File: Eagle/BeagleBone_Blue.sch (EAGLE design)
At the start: 152 parts, among them M1 JST_ZH_2, M2 JST_ZH_2, M3 JST_ZH_2, M4 JST_ZH_2, Q3 MOSFET-N, U1 OSD3358

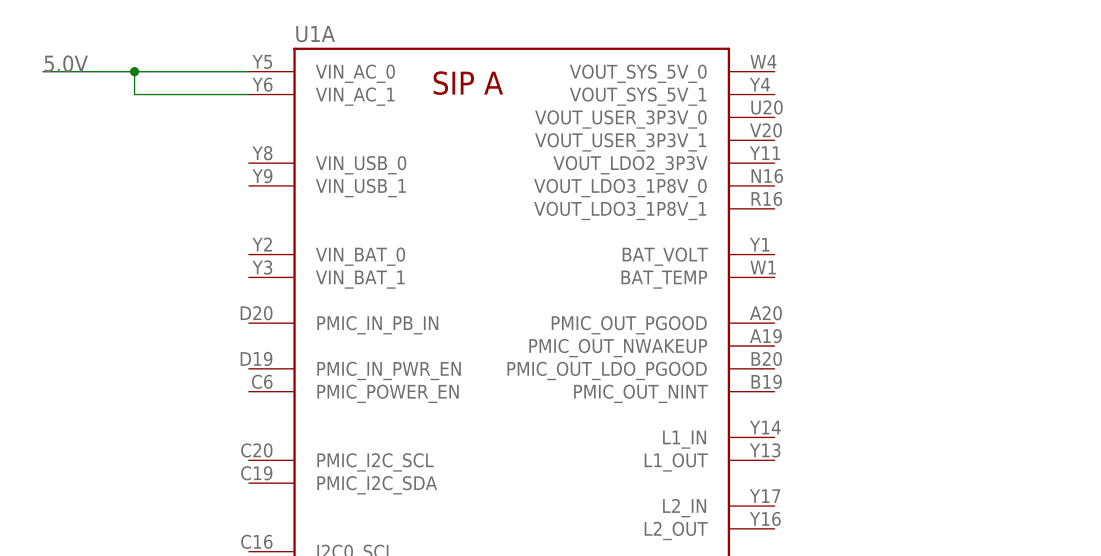
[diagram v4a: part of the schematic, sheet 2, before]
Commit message: Connected PWR button
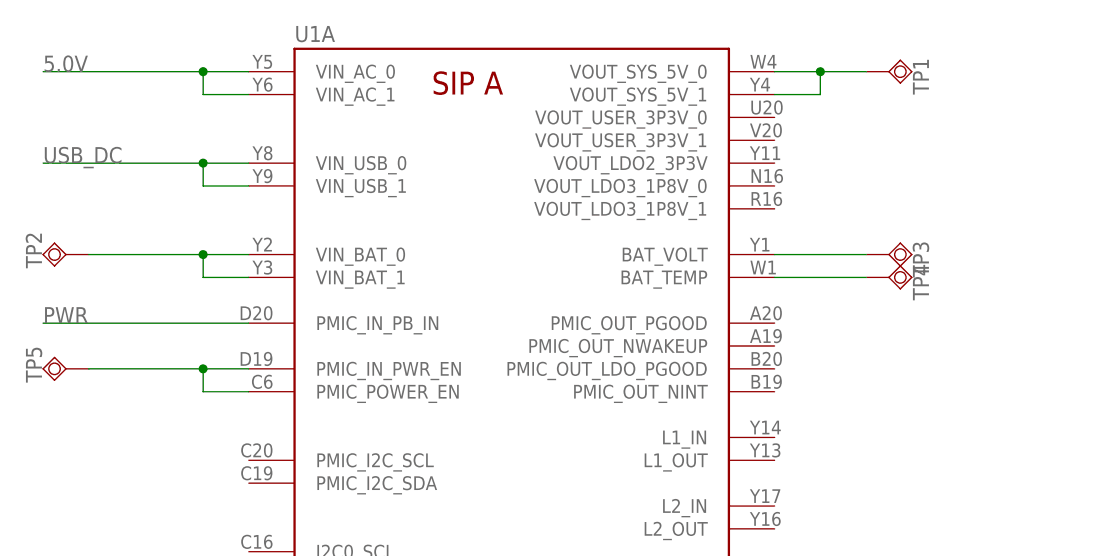
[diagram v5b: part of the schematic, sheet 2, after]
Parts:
- removed U$10, U$11, U$13, U$14, U$15, U$16, U$17, U$18, U$19, U$20, U$21, U$22, U$24, U$25, U$26, U$27, U$28, U$29, U$3, U$30, U$4, U$5, U$7: OSD3358, BeagleBone_Blue:OSD3358
- added TP1, TP2, TP3, TP4, TP5: TPSQB1,27, testpad:TPSQB1,27
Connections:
- new net N$12: TP5.TP, U1A.PMIC_IN_PWR_EN, U1A.PMIC_POWER_EN
- new net N$2: TP1.TP, U1A.VOUT_SYS_5V_0, U1A.VOUT_SYS_5V_1
- new net N$5: TP2.TP, U1A.VIN_BAT_0, U1A.VIN_BAT_1
- new net N$7: TP3.TP, U1A.BAT_VOLT
- new net N$9: TP4.TP, U1A.BAT_TEMP
- new net USB_DC: U1A.VIN_USB_0, U1A.VIN_USB_1
- net PWR: now also U1A.PMIC_IN_PB_IN
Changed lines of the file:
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@@
 <layer number="223" name="223bmp" color="24" fill="1" visible="no" active="no"/>
 <layer number="224" name="224bmp" color="25" fill="1" visible="no" active="no"/>
+<layer number="225" name="225bmp" color="7" fill="1" visible="yes" active="yes"/>
+<layer number="226" name="226bmp" color="7" fill="1" visible="yes" active="yes"/>
+<layer number="227" name="227bmp" color="7" fill="1" visible="yes" active="yes"/>
+<layer number="228" name="228bmp" color="7" fill="1" visible="yes" active="yes"/>
+<layer number="229" name="229bmp" color="7" fill="1" visible="yes" active="yes"/>
+<layer number="230" name="230bmp" color="7" fill="1" visible="yes" active="yes"/>
+<layer number="231" name="231bmp" color="7" fill="1" visible="yes" active="yes"/>
 <layer number="248" name="Housing" color="7" fill="1" visible="yes" active="yes"/>
 <layer number="249" name="Edge" color="7" fill="1" visible="yes" active="yes"/>
@@
 <layer number="251" name="SMDround" color="12" fill="11" visible="no" active="no"/>
 <layer number="254" name="cooling" color="7" fill="1" visible="yes" active="yes"/>
+<layer number="255" name="routoute" color="7" fill="1" visible="yes" active="yes"/>
 </layers>
 <schematic xreflabel="%F%N/%S.%C%R" xrefpart="/%S.%C%R">
@@
 <part name="R8" library="Strawson_Eagle_Lib" deviceset="RESISTOR" device="0402-RES" value="10k"/>
 <part name="GND9" library="SparkFun-Aesthetics" deviceset="GND" device=""/>
-<part name="U$3" library="BeagleBone_Blue" deviceset="OSD3358" device=""/>
-<part name="U$4" library="BeagleBone_Blue" deviceset="OSD3358" device=""/>
-<part name="U$5" library="BeagleBone_Blue" deviceset="OSD3358" device=""/>
-<part name="U$7" library="BeagleBone_Blue" deviceset="OSD3358" device=""/>
-<part name="U$10" library="BeagleBone_Blue" deviceset="OSD3358" device=""/>
-<part name="U$11" library="BeagleBone_Blue" deviceset="OSD3358" device=""/>
-<part name="U$13" library="BeagleBone_Blue" deviceset="OSD3358" device=""/>
-<part name="U$14" library="BeagleBone_Blue" deviceset="OSD3358" device=""/>
-<part name="U$15" library="BeagleBone_Blue" deviceset="OSD3358" device=""/>
-<part name="U$16" library="BeagleBone_Blue" deviceset="OSD3358" device=""/>
-<part name="U$17" library="BeagleBone_Blue" deviceset="OSD3358" device=""/>
-<part name="U$18" library="BeagleBone_Blue" deviceset="OSD3358" device=""/>
-<part name="U$19" library="BeagleBone_Blue" deviceset="OSD3358" device=""/>
-<part name="U$20" library="BeagleBone_Blue" deviceset="OSD3358" device=""/>
-<part name="U$21" library="BeagleBone_Blue" deviceset="OSD3358" device=""/>
-<part name="U$22" library="BeagleBone_Blue" deviceset="OSD3358" device=""/>
-<part name="U$24" library="BeagleBone_Blue" deviceset="OSD3358" device=""/>
-<part name="U$25" library="BeagleBone_Blue" deviceset="OSD3358" device=""/>
-<part name="U$26" library="BeagleBone_Blue" deviceset="OSD3358" device=""/>
-<part name="U$27" library="BeagleBone_Blue" deviceset="OSD3358" device=""/>
-<part name="U$28" library="BeagleBone_Blue" deviceset="OSD3358" device=""/>
-<part name="U$29" library="BeagleBone_Blue" deviceset="OSD3358" device=""/>
-<part name="U$30" library="BeagleBone_Blue" deviceset="OSD3358" device=""/>
 <part name="U1" library="BeagleBone_Blue" deviceset="OSD3358" device=""/>
+<part name="TP1" library="testpad" deviceset="TPSQ" device="B1,27"/>
+<part name="TP2" library="testpad" deviceset="TPSQ" device="B1,27"/>
+<part name="TP3" library="testpad" deviceset="TPSQ" device="B1,27"/>
+<part name="TP4" library="testpad" deviceset="TPSQ" device="B1,27"/>
+<part name="TP5" library="testpad" deviceset="TPSQ" device="B1,27"/>
 </parts>
 <sheets>
@@
 <instance part="U1" gate="A" x="71.12" y="187.96"/>
 <instance part="U1" gate="C" x="71.12" y="33.02"/>
+<instance part="TP1" gate="G$1" x="137.16" y="248.92" rot="R90"/>
+<instance part="TP2" gate="G$1" x="45.72" y="228.6" rot="R270"/>
+<instance part="TP3" gate="G$1" x="137.16" y="228.6" rot="R90"/>
+<instance part="TP4" gate="G$1" x="137.16" y="226.06" rot="R90"/>
+<instance part="TP5" gate="G$1" x="45.72" y="215.9" rot="R270"/>
 </instances>
 <busses>
@@
 <segment>
 <pinref part="U1" gate="A" pin="VIN_AC_0"/>
-<wire x1="66.04" y1="248.92" x2="53.34" y2="248.92" width="0.1524" layer="91"/>
-<wire x1="53.34" y1="248.92" x2="53.34" y2="246.38" width="0.1524" layer="91"/>
+<wire x1="66.04" y1="248.92" x2="60.96" y2="248.92" width="0.1524" layer="91"/>
+<wire x1="60.96" y1="248.92" x2="60.96" y2="246.38" width="0.1524" layer="91"/>
 <pinref part="U1" gate="A" pin="VIN_AC_1"/>
-<wire x1="53.34" y1="246.38" x2="66.04" y2="246.38" width="0.1524" layer="91"/>
-<wire x1="53.34" y1="248.92" x2="43.18" y2="248.92" width="0.1524" layer="91"/>
-<junction x="53.34" y="248.92"/>
+<wire x1="60.96" y1="246.38" x2="66.04" y2="246.38" width="0.1524" layer="91"/>
+<wire x1="60.96" y1="248.92" x2="43.18" y2="248.92" width="0.1524" layer="91"/>
+<junction x="60.96" y="248.92"/>
 <label x="43.18" y="248.92" size="1.778" layer="95"/>
 </segment>
 </net>
+<net name="N$2" class="0">
+<segment>
+<pinref part="U1" gate="A" pin="VOUT_SYS_5V_1"/>
+<wire x1="124.46" y1="246.38" x2="129.54" y2="246.38" width="0.1524" layer="91"/>
+<wire x1="129.54" y1="246.38" x2="129.54" y2="248.92" width="0.1524" layer="91"/>
+<pinref part="U1" gate="A" pin="VOUT_SYS_5V_0"/>
+<wire x1="129.54" y1="248.92" x2="124.46" y2="248.92" width="0.1524" layer="91"/>
+<wire x1="129.54" y1="248.92" x2="134.62" y2="248.92" width="0.1524" layer="91"/>
+<junction x="129.54" y="248.92"/>
+<pinref part="TP1" gate="G$1" pin="TP"/>
+</segment>
+</net>
+<net name="USB_DC" class="0">
+<segment>
+<pinref part="U1" gate="A" pin="VIN_USB_0"/>
+<wire x1="66.04" y1="238.76" x2="60.96" y2="238.76" width="0.1524" layer="91"/>
+<pinref part="U1" gate="A" pin="VIN_USB_1"/>
+<wire x1="60.96" y1="238.76" x2="43.18" y2="238.76" width="0.1524" layer="91"/>
+<wire x1="66.04" y1="236.22" x2="60.96" y2="236.22" width="0.1524" layer="91"/>
+<wire x1="60.96" y1="236.22" x2="60.96" y2="238.76" width="0.1524" layer="91"/>
+<junction x="60.96" y="238.76"/>
+<label x="43.18" y="238.76" size="1.778" layer="95"/>
+</segment>
+</net>
+<net name="N$5" class="0">
+<segment>
+<pinref part="U1" gate="A" pin="VIN_BAT_0"/>
+<wire x1="66.04" y1="228.6" x2="60.96" y2="228.6" width="0.1524" layer="91"/>
+<wire x1="60.96" y1="228.6" x2="48.26" y2="228.6" width="0.1524" layer="91"/>
+<wire x1="60.96" y1="228.6" x2="60.96" y2="226.06" width="0.1524" layer="91"/>
+<junction x="60.96" y="228.6"/>
+<pinref part="U1" gate="A" pin="VIN_BAT_1"/>
+<wire x1="60.96" y1="226.06" x2="66.04" y2="226.06" width="0.1524" layer="91"/>
+<pinref part="TP2" gate="G$1" pin="TP"/>
+</segment>
+</net>
+<net name="N$7" class="0">
+<segment>
+<pinref part="U1" gate="A" pin="BAT_VOLT"/>
+<pinref part="TP3" gate="G$1" pin="TP"/>
+<wire x1="124.46" y1="228.6" x2="134.62" y2="228.6" width="0.1524" layer="91"/>
+</segment>
+</net>
+<net name="N$9" class="0">
+<segment>
+<pinref part="U1" gate="A" pin="BAT_TEMP"/>
+<pinref part="TP4" gate="G$1" pin="TP"/>
+<wire x1="124.46" y1="226.06" x2="134.62" y2="226.06" width="0.1524" layer="91"/>
+</segment>
+</net>
+<net name="N$12" class="0">
+<segment>
+<pinref part="U1" gate="A" pin="PMIC_IN_PWR_EN"/>
+<wire x1="66.04" y1="215.9" x2="60.96" y2="215.9" width="0.1524" layer="91"/>
+<wire x1="60.96" y1="215.9" x2="48.26" y2="215.9" width="0.1524" layer="91"/>
+<wire x1="60.96" y1="215.9" x2="60.96" y2="213.36" width="0.1524" layer="91"/>
+<junction x="60.96" y="215.9"/>
+<pinref part="U1" gate="A" pin="PMIC_POWER_EN"/>
+<wire x1="60.96" y1="213.36" x2="66.04" y2="213.36" width="0.1524" layer="91"/>
+<pinref part="TP5" gate="G$1" pin="TP"/>
+</segment>
+</net>
+<net name="PWR" class="0">
+<segment>
+<pinref part="U1" gate="A" pin="PMIC_IN_PB_IN"/>
+<wire x1="66.04" y1="220.98" x2="43.18" y2="220.98" width="0.1524" layer="91"/>
+<label x="43.18" y="220.98" size="1.778" layer="95"/>
+</segment>
+</net>

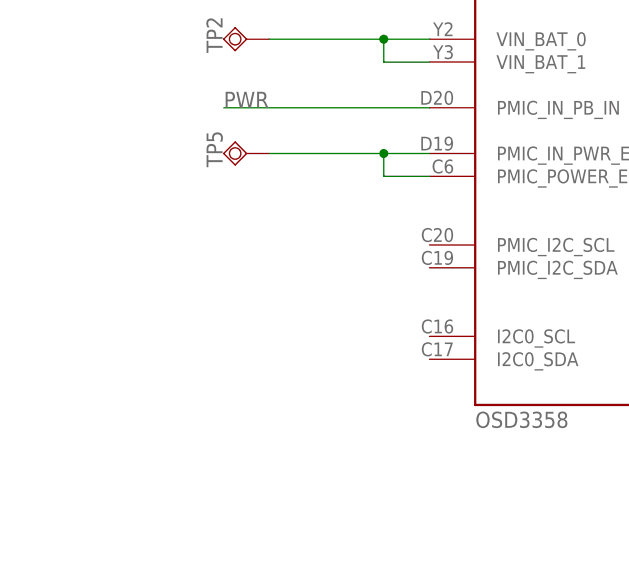
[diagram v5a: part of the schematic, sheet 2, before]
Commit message: Connected I2C2, but not EEPROM
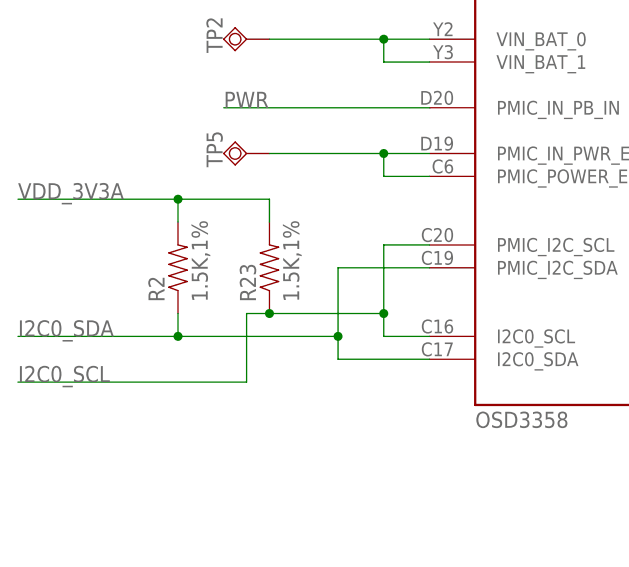
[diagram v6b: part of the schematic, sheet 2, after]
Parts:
- added R2, R23: 1.5K,1%, Strawson_Eagle_Lib:RESISTOR0402-RES
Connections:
- new net I2C0_SCL: R23.1, U1A.I2C0_SCL, U1A.PMIC_I2C_SCL
- new net I2C0_SDA: R2.1, U1A.I2C0_SDA, U1A.PMIC_I2C_SDA
- new net VDD_3V3A: R2.2, R23.2
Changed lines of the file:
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@@
 <layer number="56" name="wert" color="7" fill="1" visible="no" active="no"/>
 <layer number="57" name="tCAD" color="7" fill="1" visible="no" active="no"/>
+<layer number="59" name="tCarbon" color="7" fill="1" visible="no" active="no"/>
+<layer number="60" name="bCarbon" color="7" fill="1" visible="no" active="no"/>
 <layer number="90" name="Modules" color="5" fill="1" visible="yes" active="yes"/>
 <layer number="91" name="Nets" color="2" fill="1" visible="yes" active="yes"/>
@@
 <layer number="113" name="IDFDebug" color="4" fill="1" visible="yes" active="yes"/>
 <layer number="114" name="GND" color="11" fill="1" visible="yes" active="yes"/>
+<layer number="115" name="ReferenceISLANDS" color="7" fill="1" visible="yes" active="yes"/>
 <layer number="116" name="Patch_BOT" color="9" fill="4" visible="yes" active="yes"/>
+<layer number="118" name="Rect_Pads" color="7" fill="1" visible="yes" active="yes"/>
 <layer number="121" name="_tsilk" color="7" fill="1" visible="yes" active="yes"/>
 <layer number="122" name="_bsilk" color="7" fill="1" visible="yes" active="yes"/>
@@
 <layer number="127" name="_tValues" color="7" fill="1" visible="yes" active="yes"/>
 <layer number="128" name="_bValues" color="7" fill="1" visible="yes" active="yes"/>
+<layer number="129" name="Mask" color="7" fill="1" visible="yes" active="yes"/>
 <layer number="131" name="tAdjust" color="7" fill="1" visible="yes" active="yes"/>
 <layer number="132" name="bAdjust" color="7" fill="1" visible="yes" active="yes"/>
@@
 <part name="TP4" library="testpad" deviceset="TPSQ" device="B1,27"/>
 <part name="TP5" library="testpad" deviceset="TPSQ" device="B1,27"/>
+<part name="R2" library="Strawson_Eagle_Lib" deviceset="RESISTOR" device="0402-RES" value="1.5K,1%"/>
+<part name="R23" library="Strawson_Eagle_Lib" deviceset="RESISTOR" device="0402-RES" value="1.5K,1%"/>
 </parts>
 <sheets>
@@
 <instance part="TP4" gate="G$1" x="137.16" y="226.06" rot="R90"/>
 <instance part="TP5" gate="G$1" x="45.72" y="215.9" rot="R270"/>
+<instance part="R2" gate="G$1" x="38.1" y="203.2" rot="R90"/>
+<instance part="R23" gate="G$1" x="48.26" y="203.2" rot="R90"/>
 </instances>
 <busses>
@@
 </segment>
 </net>
+<net name="I2C0_SCL" class="0">
+<segment>
+<pinref part="U1" gate="A" pin="I2C0_SCL"/>
+<wire x1="66.04" y1="195.58" x2="60.96" y2="195.58" width="0.1524" layer="91"/>
+<wire x1="60.96" y1="195.58" x2="60.96" y2="198.12" width="0.1524" layer="91"/>
+<pinref part="U1" gate="A" pin="PMIC_I2C_SCL"/>
+<wire x1="60.96" y1="198.12" x2="60.96" y2="205.74" width="0.1524" layer="91"/>
+<wire x1="60.96" y1="205.74" x2="66.04" y2="205.74" width="0.1524" layer="91"/>
+<pinref part="R23" gate="G$1" pin="1"/>
+<wire x1="48.26" y1="198.12" x2="60.96" y2="198.12" width="0.1524" layer="91"/>
+<junction x="60.96" y="198.12"/>
+<wire x1="48.26" y1="198.12" x2="45.72" y2="198.12" width="0.1524" layer="91"/>
+<wire x1="45.72" y1="198.12" x2="45.72" y2="190.5" width="0.1524" layer="91"/>
+<junction x="48.26" y="198.12"/>
+<wire x1="45.72" y1="190.5" x2="20.32" y2="190.5" width="0.1524" layer="91"/>
+<label x="20.32" y="190.5" size="1.778" layer="95"/>
+</segment>
+</net>
+<net name="I2C0_SDA" class="0">
+<segment>
+<pinref part="U1" gate="A" pin="PMIC_I2C_SDA"/>
+<wire x1="66.04" y1="203.2" x2="55.88" y2="203.2" width="0.1524" layer="91"/>
+<wire x1="55.88" y1="203.2" x2="55.88" y2="195.58" width="0.1524" layer="91"/>
+<pinref part="U1" gate="A" pin="I2C0_SDA"/>
+<wire x1="55.88" y1="195.58" x2="55.88" y2="193.04" width="0.1524" layer="91"/>
+<wire x1="55.88" y1="193.04" x2="66.04" y2="193.04" width="0.1524" layer="91"/>
+<pinref part="R2" gate="G$1" pin="1"/>
+<wire x1="38.1" y1="198.12" x2="38.1" y2="195.58" width="0.1524" layer="91"/>
+<wire x1="38.1" y1="195.58" x2="55.88" y2="195.58" width="0.1524" layer="91"/>
+<junction x="55.88" y="195.58"/>
+<wire x1="38.1" y1="195.58" x2="20.32" y2="195.58" width="0.1524" layer="91"/>
+<junction x="38.1" y="195.58"/>
+<label x="20.32" y="195.58" size="1.778" layer="95"/>
+</segment>
+</net>
+<net name="VDD_3V3A" class="0">
+<segment>
+<pinref part="R2" gate="G$1" pin="2"/>
+<wire x1="38.1" y1="208.28" x2="38.1" y2="210.82" width="0.1524" layer="91"/>
+<wire x1="20.32" y1="210.82" x2="38.1" y2="210.82" width="0.1524" layer="91"/>
+<pinref part="R23" gate="G$1" pin="2"/>
+<wire x1="38.1" y1="210.82" x2="48.26" y2="210.82" width="0.1524" layer="91"/>
+<wire x1="48.26" y1="210.82" x2="48.26" y2="208.28" width="0.1524" layer="91"/>
+<junction x="38.1" y="210.82"/>
+<label x="20.32" y="210.82" size="1.778" layer="95"/>
+</segment>
+</net>

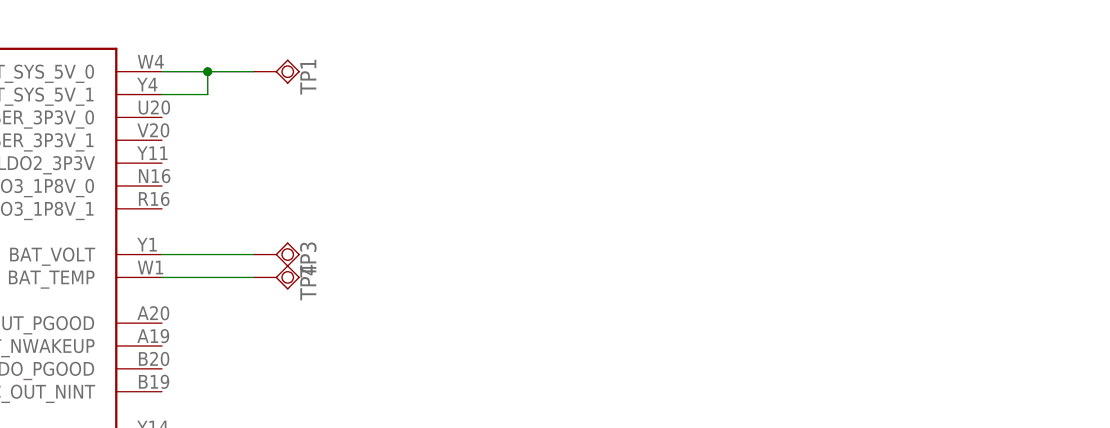
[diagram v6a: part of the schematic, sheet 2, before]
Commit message: Add PWR_LEDR LED
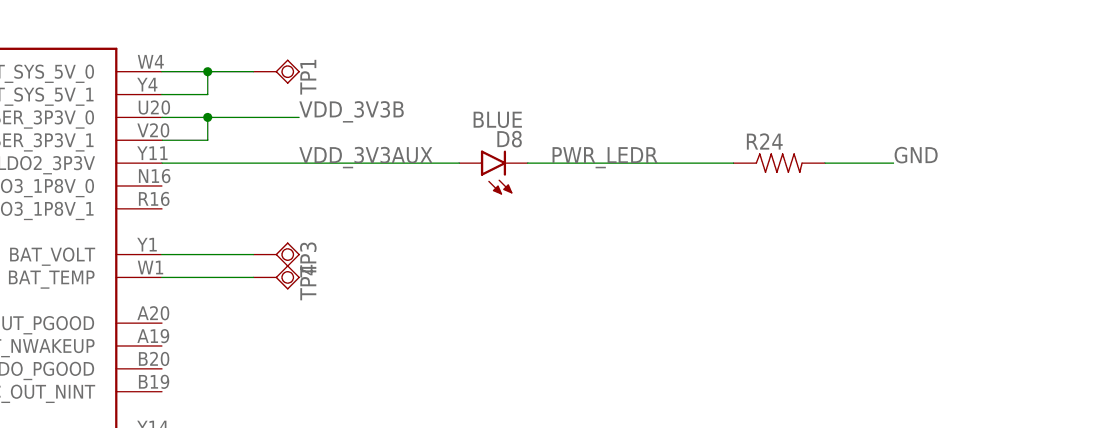
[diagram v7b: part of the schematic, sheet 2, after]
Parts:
- added D8: BLUE, BeagleBone_Blue:LED0603
- added R24: (no value), Strawson_Eagle_Lib:RESISTOR0402-RES
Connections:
- new net PWR_LEDR: D8.C, R24.1
- new net VDD_3V3AUX: D8.A, U1A.VOUT_LDO2_3P3V
- new net VDD_3V3B: U1A.VOUT_USER_3P3V_0, U1A.VOUT_USER_3P3V_1
- net GND: now also R24.2
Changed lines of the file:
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@@
 <part name="R2" library="Strawson_Eagle_Lib" deviceset="RESISTOR" device="0402-RES" value="1.5K,1%"/>
 <part name="R23" library="Strawson_Eagle_Lib" deviceset="RESISTOR" device="0402-RES" value="1.5K,1%"/>
+<part name="D8" library="BeagleBone_Blue" deviceset="LED" device="0603" value="BLUE"/>
+<part name="R24" library="Strawson_Eagle_Lib" deviceset="RESISTOR" device="0402-RES"/>
 </parts>
 <sheets>
@@
 <instance part="R2" gate="G$1" x="38.1" y="203.2" rot="R90"/>
 <instance part="R23" gate="G$1" x="48.26" y="203.2" rot="R90"/>
+<instance part="D8" gate="G$1" x="160.02" y="238.76" rot="R90"/>
+<instance part="R24" gate="G$1" x="193.04" y="238.76"/>
 </instances>
 <busses>
@@
 </segment>
 </net>
+<net name="VDD_3V3B" class="0">
+<segment>
+<pinref part="U1" gate="A" pin="VOUT_USER_3P3V_0"/>
+<wire x1="124.46" y1="243.84" x2="129.54" y2="243.84" width="0.1524" layer="91"/>
+<pinref part="U1" gate="A" pin="VOUT_USER_3P3V_1"/>
+<wire x1="129.54" y1="243.84" x2="139.7" y2="243.84" width="0.1524" layer="91"/>
+<wire x1="124.46" y1="241.3" x2="129.54" y2="241.3" width="0.1524" layer="91"/>
+<wire x1="129.54" y1="241.3" x2="129.54" y2="243.84" width="0.1524" layer="91"/>
+<junction x="129.54" y="243.84"/>
+<label x="139.7" y="243.84" size="1.778" layer="95"/>
+</segment>
+</net>
+<net name="VDD_3V3AUX" class="0">
+<segment>
+<pinref part="U1" gate="A" pin="VOUT_LDO2_3P3V"/>
+<wire x1="124.46" y1="238.76" x2="157.48" y2="238.76" width="0.1524" layer="91"/>
+<label x="139.7" y="238.76" size="1.778" layer="95"/>
+<pinref part="D8" gate="G$1" pin="A"/>
+</segment>
+</net>
+<net name="PWR_LEDR" class="0">
+<segment>
+<pinref part="D8" gate="G$1" pin="C"/>
+<pinref part="R24" gate="G$1" pin="1"/>
+<wire x1="165.1" y1="238.76" x2="187.96" y2="238.76" width="0.1524" layer="91"/>
+<label x="167.64" y="238.76" size="1.778" layer="95"/>
+</segment>
+</net>
+<net name="GND" class="0">
+<segment>
+<pinref part="R24" gate="G$1" pin="2"/>
+<wire x1="198.12" y1="238.76" x2="205.74" y2="238.76" width="0.1524" layer="91"/>
+<label x="205.74" y="238.76" size="1.778" layer="95"/>
+</segment>
+</net>
